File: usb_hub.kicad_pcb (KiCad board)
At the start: 2 copper layers, 100 x 50 mm, 96 parts, among them J1 Barrel_Jack_Switch, J2 USB_A, J3 USB_A, J4 USB_A, J5 USB_A, J6 Conn_01x04, J7 Conn_02x03_Odd_Even, J8 Conn_01x04, SW1 SW_DIP_x01, SW2 SW_Push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

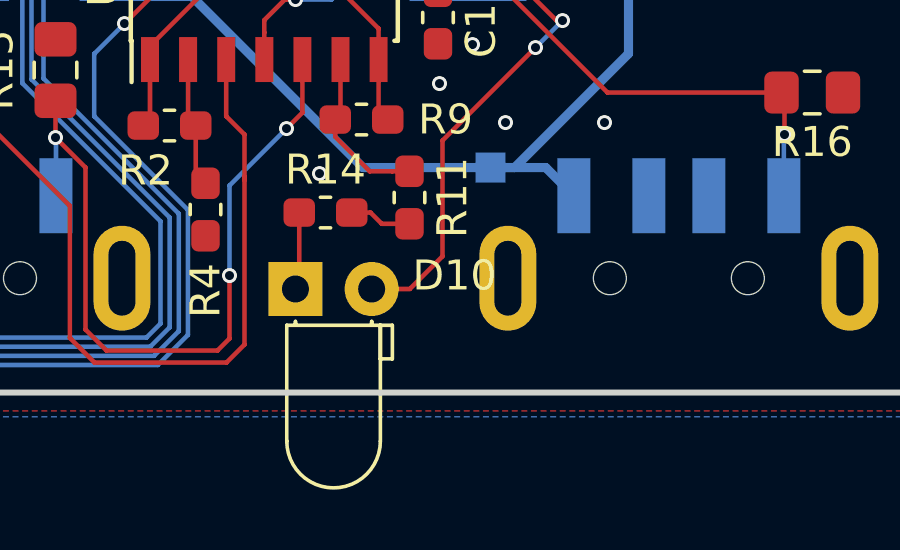
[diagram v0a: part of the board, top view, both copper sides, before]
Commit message: Fixing USB conn. gender and others: * 5V supply is simplified in one controller (55W); * Each USB port has it's on Current/Mode controller;
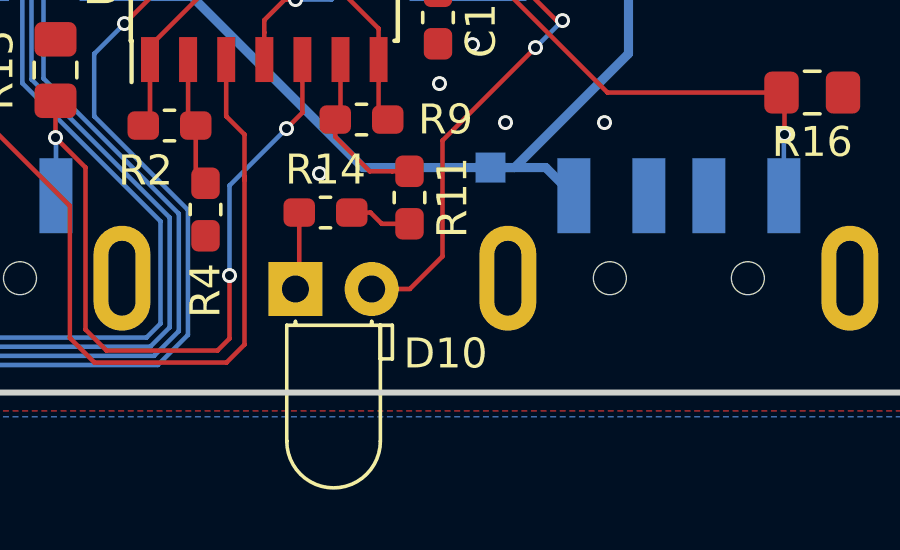
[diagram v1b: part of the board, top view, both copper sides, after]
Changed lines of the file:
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@@
     (descr "LED, diameter 3.0mm z-position of LED center 2.0mm, 2 pins")
     (tags "LED diameter 3.0mm z-position of LED center 2.0mm 2 pins")
-    (fp_text reference D10 (at 5.301 -0.448) (layer F.SilkS)
+    (fp_text reference D10 (at 5.001 2.152) (layer F.SilkS)
       (effects (font (size 1 1) (thickness 0.15)))
     )
